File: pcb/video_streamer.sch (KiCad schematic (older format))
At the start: 0 parts

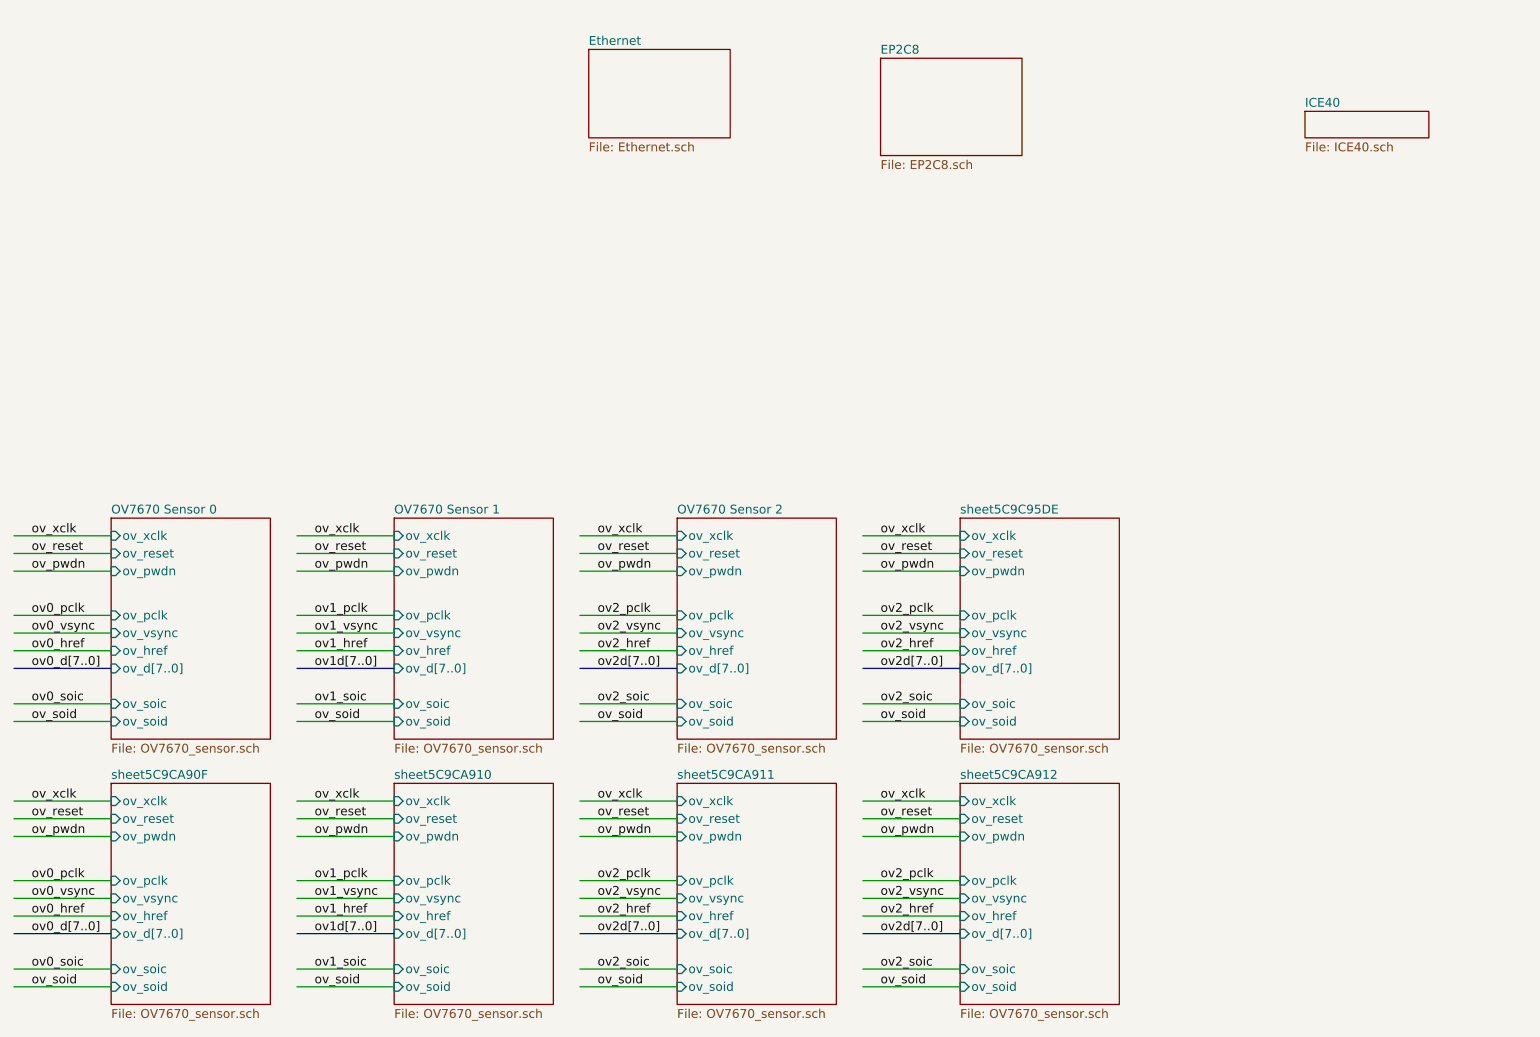
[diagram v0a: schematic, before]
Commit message: OV flat footprint
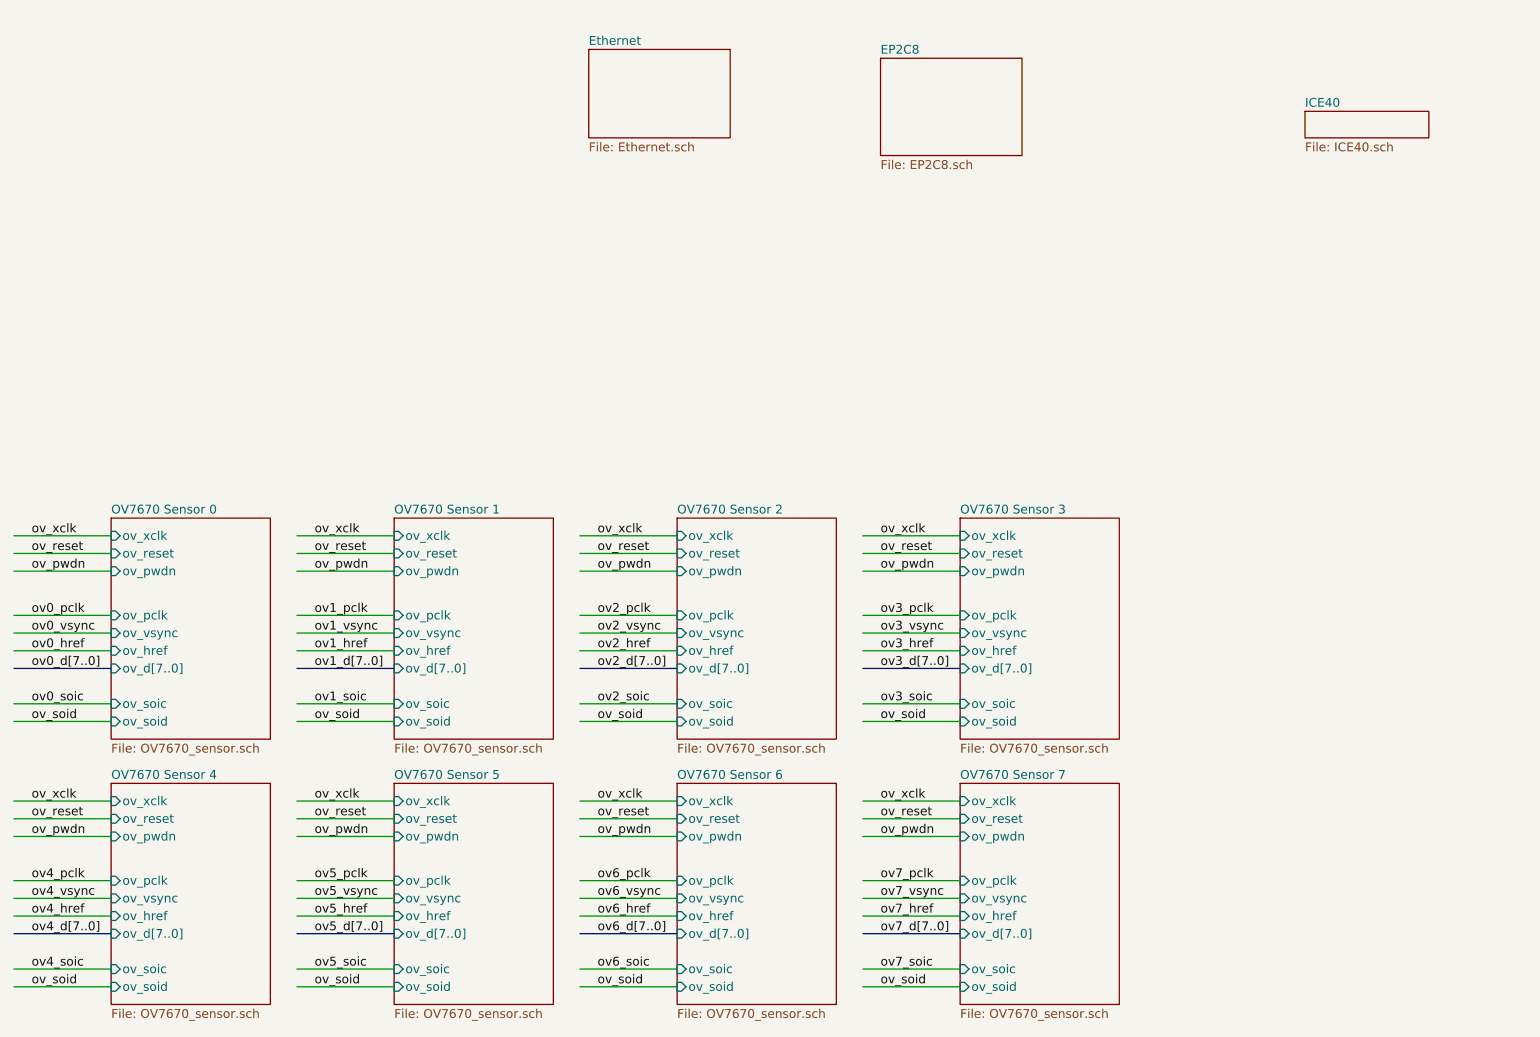
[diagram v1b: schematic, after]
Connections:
- net labels added: ov1_d[7..0], ov2_d[7..0], ov3_d[7..0], ov3_href, ov3_pclk, ov3_soic, ov3_vsync, ov4_d[7..0], ov4_href, ov4_pclk, ov4_soic, ov4_vsync, ov5_d[7..0], ov5_href, ov5_pclk, ov5_soic, ov5_vsync, ov6_d[7..0], ov6_href, ov6_pclk, ov6_soic, ov6_vsync, ov7_d[7..0], ov7_href, ov7_pclk, ov7_soic, ov7_vsync
- net labels removed: ov1d[7..0], ov2d[7..0]
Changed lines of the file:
@@
 	3000 4450 2450 4450
 Text Label 2550 4450 0    50   ~ 0
-ov1d[7..0]
+ov1_d[7..0]
 Wire Wire Line
 	3000 4650 2450 4650
@@
 	4600 4450 4050 4450
 Text Label 4150 4450 0    50   ~ 0
-ov2d[7..0]
+ov2_d[7..0]
 Wire Wire Line
 	4600 4650 4050 4650
@@
 S 6200 3600 900  1250
 U 5C9C95E9
-F0 "sheet5C9C95DE" 50
+F0 "OV7670 Sensor 3" 50
 F1 "OV7670_sensor.sch" 50
 F2 "ov_pclk" I L 6200 4150 50
@@
 	6200 4150 5650 4150
 Text Label 5750 4150 0    50   ~ 0
-ov2_pclk
+ov3_pclk
 Wire Wire Line
 	6200 4250 5650 4250
 Text Label 5750 4250 0    50   ~ 0
-ov2_vsync
+ov3_vsync
 Wire Wire Line
 	6200 4350 5650 4350
 Text Label 5750 4350 0    50   ~ 0
-ov2_href
+ov3_href
 Wire Bus Line
 	6200 4450 5650 4450
 Text Label 5750 4450 0    50   ~ 0
-ov2d[7..0]
+ov3_d[7..0]
 Wire Wire Line
 	6200 4650 5650 4650
 Text Label 5750 4650 0    50   ~ 0
-ov2_soic
+ov3_soic
 Wire Wire Line
 	6200 4750 5650 4750
@@
 S 1400 5100 900  1250
 U 5C9CA91D
-F0 "sheet5C9CA90F" 50
+F0 "OV7670 Sensor 4" 50
 F1 "OV7670_sensor.sch" 50
 F2 "ov_pclk" I L 1400 5650 50
@@
 	1400 5650 850  5650
 Text Label 950  5650 0    50   ~ 0
-ov0_pclk
+ov4_pclk
 Wire Wire Line
 	1400 5750 850  5750
 Text Label 950  5750 0    50   ~ 0
-ov0_vsync
+ov4_vsync
 Wire Wire Line
 	1400 5850 850  5850
 Text Label 950  5850 0    50   ~ 0
-ov0_href
+ov4_href
 Wire Bus Line
 	1400 5950 850  5950
 Text Label 950  5950 0    50   ~ 0
-ov0_d[7..0]
+ov4_d[7..0]
 Wire Wire Line
 	1400 6150 850  6150
 Text Label 950  6150 0    50   ~ 0
-ov0_soic
+ov4_soic
 Wire Wire Line
 	1400 6250 850  6250
@@
 S 3000 5100 900  1250
 U 5C9CA93A
-F0 "sheet5C9CA910" 50
+F0 "OV7670 Sensor 5" 50
 F1 "OV7670_sensor.sch" 50
 F2 "ov_pclk" I L 3000 5650 50
@@
 	3000 5650 2450 5650
 Text Label 2550 5650 0    50   ~ 0
-ov1_pclk
+ov5_pclk
 Wire Wire Line
 	3000 5750 2450 5750
 Text Label 2550 5750 0    50   ~ 0
-ov1_vsync
+ov5_vsync
 Wire Wire Line
 	3000 5850 2450 5850
 Text Label 2550 5850 0    50   ~ 0
-ov1_href
+ov5_href
 Wire Bus Line
 	3000 5950 2450 5950
 Text Label 2550 5950 0    50   ~ 0
-ov1d[7..0]
+ov5_d[7..0]
 Wire Wire Line
 	3000 6150 2450 6150
 Text Label 2550 6150 0    50   ~ 0
-ov1_soic
+ov5_soic
 Wire Wire Line
 	3000 6250 2450 6250
@@
 S 4600 5100 900  1250
 U 5C9CA957
-F0 "sheet5C9CA911" 50
+F0 "OV7670 Sensor 6" 50
 F1 "OV7670_sensor.sch" 50
 F2 "ov_pclk" I L 4600 5650 50
@@
 	4600 5650 4050 5650
 Text Label 4150 5650 0    50   ~ 0
-ov2_pclk
+ov6_pclk
 Wire Wire Line
 	4600 5750 4050 5750
 Text Label 4150 5750 0    50   ~ 0
-ov2_vsync
+ov6_vsync
 Wire Wire Line
 	4600 5850 4050 5850
 Text Label 4150 5850 0    50   ~ 0
-ov2_href
+ov6_href
 Wire Bus Line
 	4600 5950 4050 5950
 Text Label 4150 5950 0    50   ~ 0
-ov2d[7..0]
+ov6_d[7..0]
 Wire Wire Line
 	4600 6150 4050 6150
 Text Label 4150 6150 0    50   ~ 0
-ov2_soic
+ov6_soic
 Wire Wire Line
 	4600 6250 4050 6250
@@
 S 6200 5100 900  1250
 U 5C9CA974
-F0 "sheet5C9CA912" 50
+F0 "OV7670 Sensor 7" 50
 F1 "OV7670_sensor.sch" 50
 F2 "ov_pclk" I L 6200 5650 50
@@
 	6200 5650 5650 5650
 Text Label 5750 5650 0    50   ~ 0
-ov2_pclk
+ov7_pclk
 Wire Wire Line
 	6200 5750 5650 5750
 Text Label 5750 5750 0    50   ~ 0
-ov2_vsync
+ov7_vsync
 Wire Wire Line
 	6200 5850 5650 5850
 Text Label 5750 5850 0    50   ~ 0
-ov2_href
+ov7_href
 Wire Bus Line
 	6200 5950 5650 5950
 Text Label 5750 5950 0    50   ~ 0
-ov2d[7..0]
+ov7_d[7..0]
 Wire Wire Line
 	6200 6150 5650 6150
 Text Label 5750 6150 0    50   ~ 0
-ov2_soic
+ov7_soic
 Wire Wire Line
 	6200 6250 5650 6250

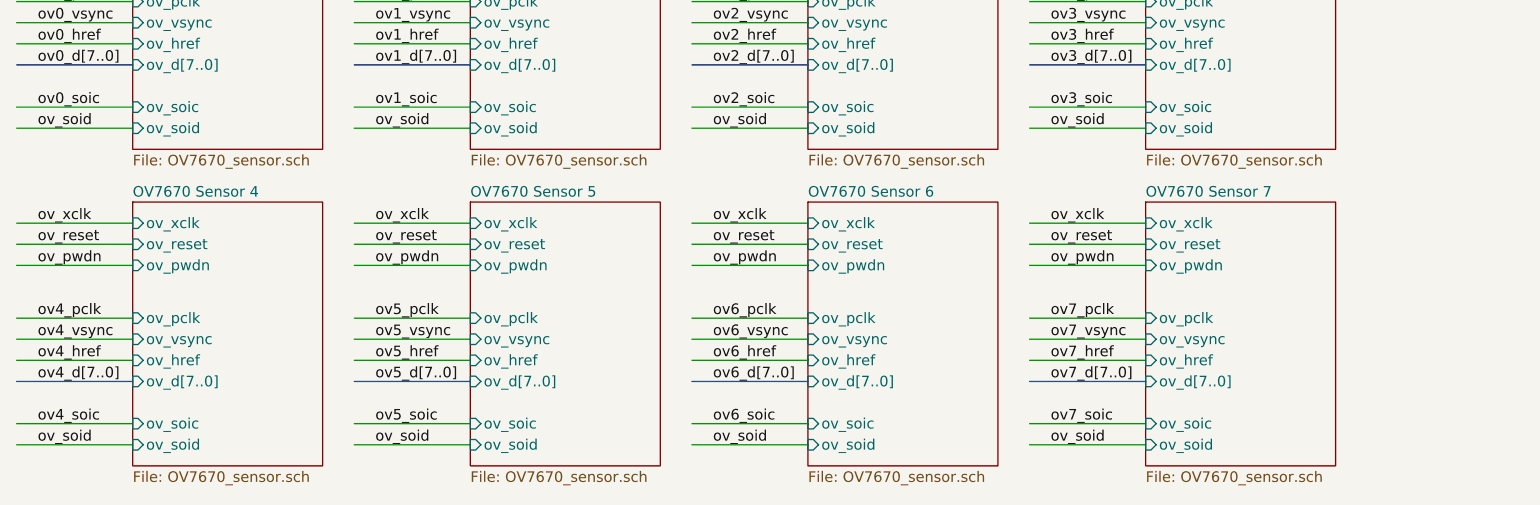
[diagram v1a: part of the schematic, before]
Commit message: Remove one flat sensor site.
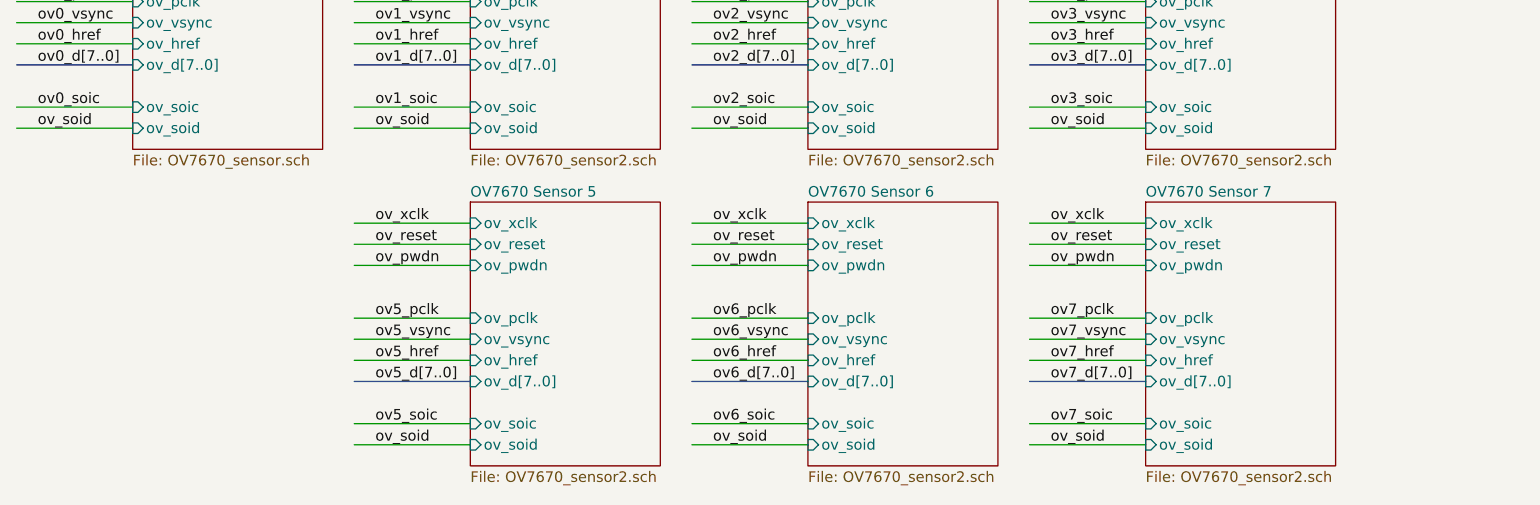
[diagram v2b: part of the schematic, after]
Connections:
- net labels removed: ov4_d[7..0], ov4_href, ov4_pclk, ov4_soic, ov4_vsync
- wire segments 64 -> 56
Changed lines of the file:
@@
 $Descr A4 11693 8268
 encoding utf-8
-Sheet 1 12
+Sheet 1 11
 Title ""
 Date ""
@@
 Comment4 ""
 $EndDescr
-$Sheet
-S 8150 1300 700  150
-U 5C67FC17
-F0 "ICE40" 50
-F1 "ICE40.sch" 50
-$EndSheet
 $Sheet
 S 4100 950  800  500
@@
 U 5C9C0506
 F0 "OV7670 Sensor 1" 50
-F1 "OV7670_sensor.sch" 50
+F1 "OV7670_sensor2.sch" 50
 F2 "ov_pclk" I L 3000 4150 50
 F3 "ov_vsync" I L 3000 4250 50
@@
 U 5C9C8588
 F0 "OV7670 Sensor 2" 50
-F1 "OV7670_sensor.sch" 50
+F1 "OV7670_sensor2.sch" 50
 F2 "ov_pclk" I L 4600 4150 50
 F3 "ov_vsync" I L 4600 4250 50
@@
 U 5C9C95E9
 F0 "OV7670 Sensor 3" 50
-F1 "OV7670_sensor.sch" 50
+F1 "OV7670_sensor2.sch" 50
 F2 "ov_pclk" I L 6200 4150 50
 F3 "ov_vsync" I L 6200 4250 50
@@
 ov_soid
 $Sheet
-S 1400 5100 900  1250
-U 5C9CA91D
-F0 "OV7670 Sensor 4" 50
-F1 "OV7670_sensor.sch" 50
-F2 "ov_pclk" I L 1400 5650 50
-F3 "ov_vsync" I L 1400 5750 50
-F4 "ov_href" I L 1400 5850 50
-F5 "ov_soic" I L 1400 6150 50
-F6 "ov_soid" I L 1400 6250 50
-F7 "ov_xclk" I L 1400 5200 50
-F8 "ov_reset" I L 1400 5300 50
-F9 "ov_pwdn" I L 1400 5400 50
-F10 "ov_d[7..0]" I L 1400 5950 50
-$EndSheet
-Wire Wire Line
-	1400 5200 850  5200
-Text Label 950  5200 0    50   ~ 0
-ov_xclk
-Wire Wire Line
-	1400 5300 850  5300
-Text Label 950  5300 0    50   ~ 0
-ov_reset
-Wire Wire Line
-	1400 5400 850  5400
-Text Label 950  5400 0    50   ~ 0
-ov_pwdn
-Wire Wire Line
-	1400 5650 850  5650
-Text Label 950  5650 0    50   ~ 0
-ov4_pclk
-Wire Wire Line
-	1400 5750 850  5750
-Text Label 950  5750 0    50   ~ 0
-ov4_vsync
-Wire Wire Line
-	1400 5850 850  5850
-Text Label 950  5850 0    50   ~ 0
-ov4_href
-Wire Bus Line
-	1400 5950 850  5950
-Text Label 950  5950 0    50   ~ 0
-ov4_d[7..0]
-Wire Wire Line
-	1400 6150 850  6150
-Text Label 950  6150 0    50   ~ 0
-ov4_soic
-Wire Wire Line
-	1400 6250 850  6250
-Text Label 950  6250 0    50   ~ 0
-ov_soid
-$Sheet
 S 3000 5100 900  1250
 U 5C9CA93A
 F0 "OV7670 Sensor 5" 50
-F1 "OV7670_sensor.sch" 50
+F1 "OV7670_sensor2.sch" 50
 F2 "ov_pclk" I L 3000 5650 50
 F3 "ov_vsync" I L 3000 5750 50
@@
 U 5C9CA957
 F0 "OV7670 Sensor 6" 50
-F1 "OV7670_sensor.sch" 50
+F1 "OV7670_sensor2.sch" 50
 F2 "ov_pclk" I L 4600 5650 50
 F3 "ov_vsync" I L 4600 5750 50
@@
 U 5C9CA974
 F0 "OV7670 Sensor 7" 50
-F1 "OV7670_sensor.sch" 50
+F1 "OV7670_sensor2.sch" 50
 F2 "ov_pclk" I L 6200 5650 50
 F3 "ov_vsync" I L 6200 5750 50
@@
 Text Label 5750 6250 0    50   ~ 0
 ov_soid
+$Sheet
+S 8150 1300 700  150
+U 5C67FC17
+F0 "ICE40" 50
+F1 "ICE40.sch" 50
+$EndSheet
 $EndSCHEMATC
